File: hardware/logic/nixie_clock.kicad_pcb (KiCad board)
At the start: 2 copper layers, 86 parts, among them J1 Conn_01x06_Pin, J2 Conn_01x04, J3 Conn_02x05_Odd_Even, J4 USB_C_PD, Q1 2N7002NXAKR, Q2 DMP3098LSD-13, SW1 SW_Push, SW2 SW_Push, SW3 SW_Push, SW4 SW_Push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

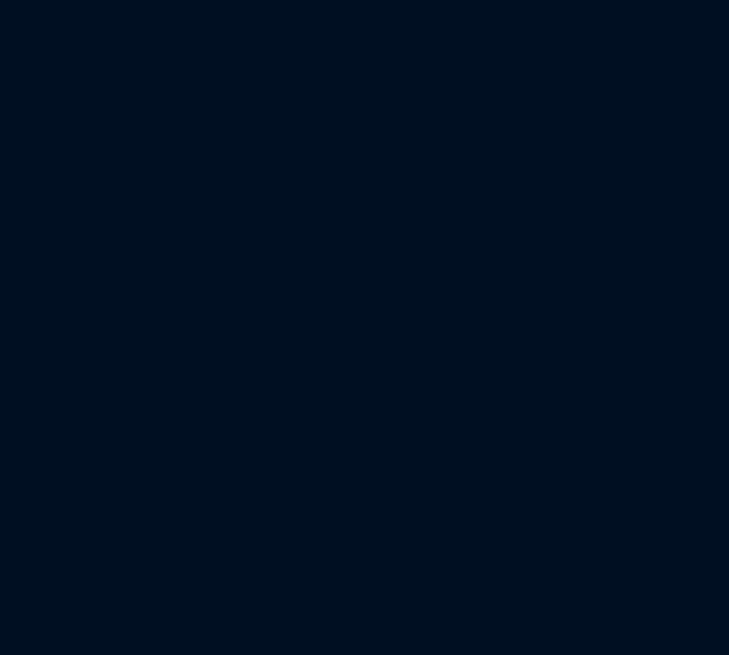
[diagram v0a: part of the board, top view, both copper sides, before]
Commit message: Changed connectors to driver board, fixed oscillator connections
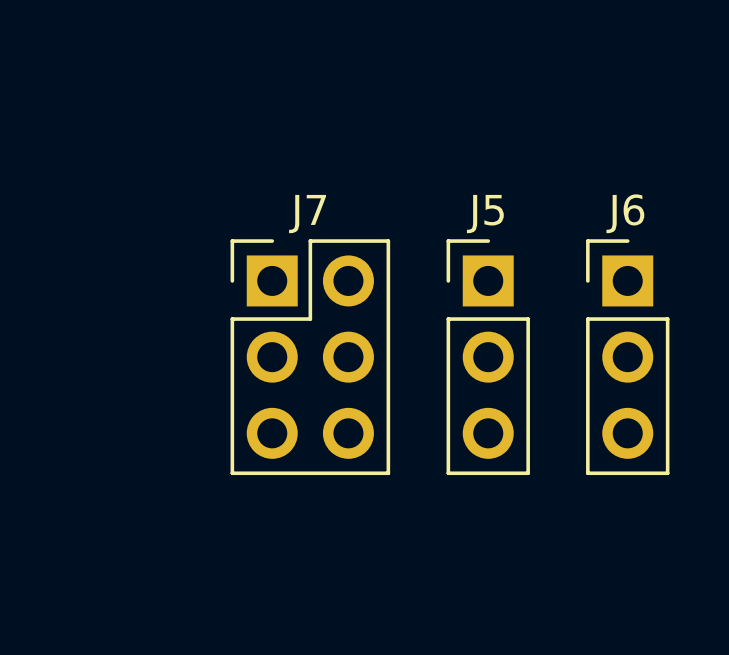
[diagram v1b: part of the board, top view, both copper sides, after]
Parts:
- added J5: Conn_01x03, Connector_PinHeader_2.54mm:PinHeader_1x03_P2.54mm_Vertical, F.Cu at (114.7, 27.9)
- added J6: Conn_01x03, Connector_PinHeader_2.54mm:PinHeader_1x03_P2.54mm_Vertical, F.Cu at (119.4, 27.9)
- added J7: Conn_02x03_Odd_Even, Connector_PinHeader_2.54mm:PinHeader_2x03_P2.54mm_Vertical, F.Cu at (107.5, 27.9)
- R13: value 1k -> 2k2
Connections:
- Y1 pad 2: /nixie_clock-MCU/HSE_IN -> GND
- Y1 pad 3: (no net) -> /nixie_clock-MCU/HSE_IN
- Y1 pad 4: (no net) -> GND

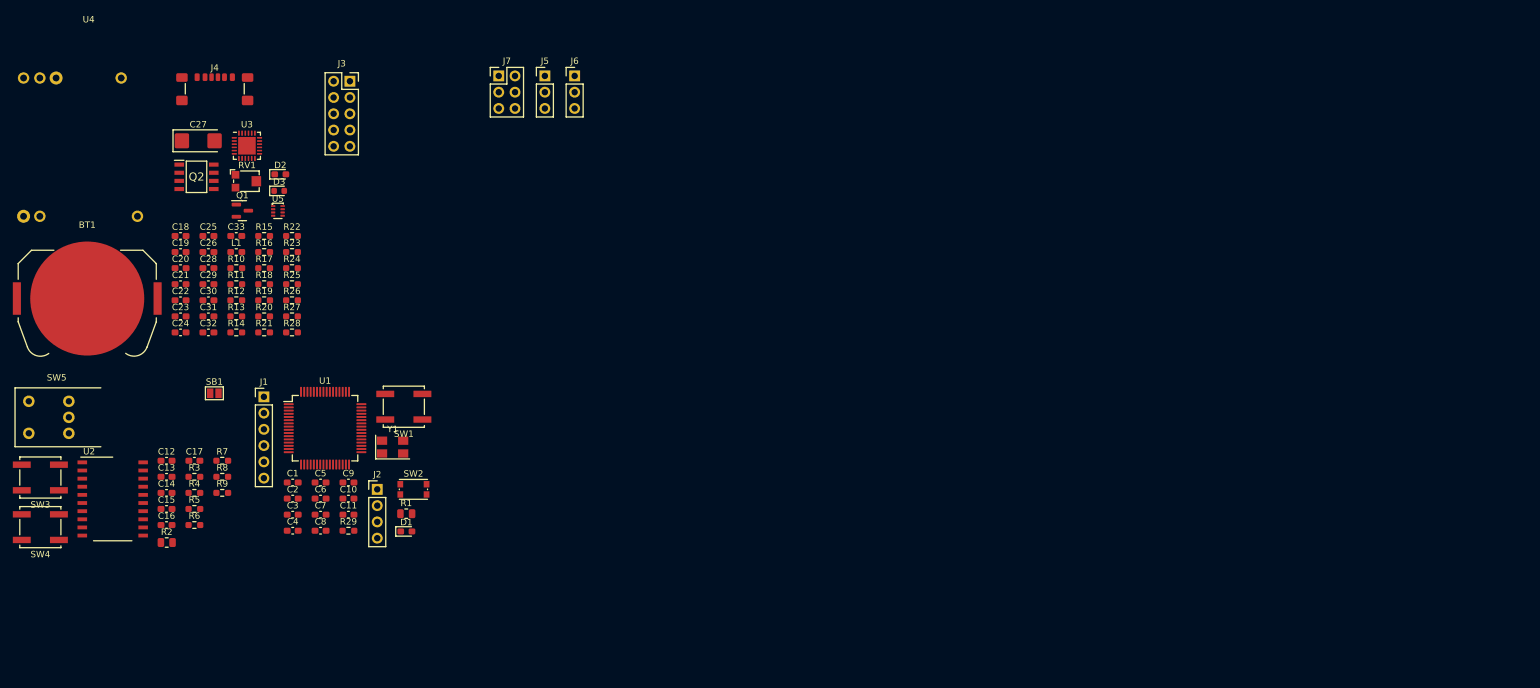
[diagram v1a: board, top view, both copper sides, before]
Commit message: Inital PCB placement
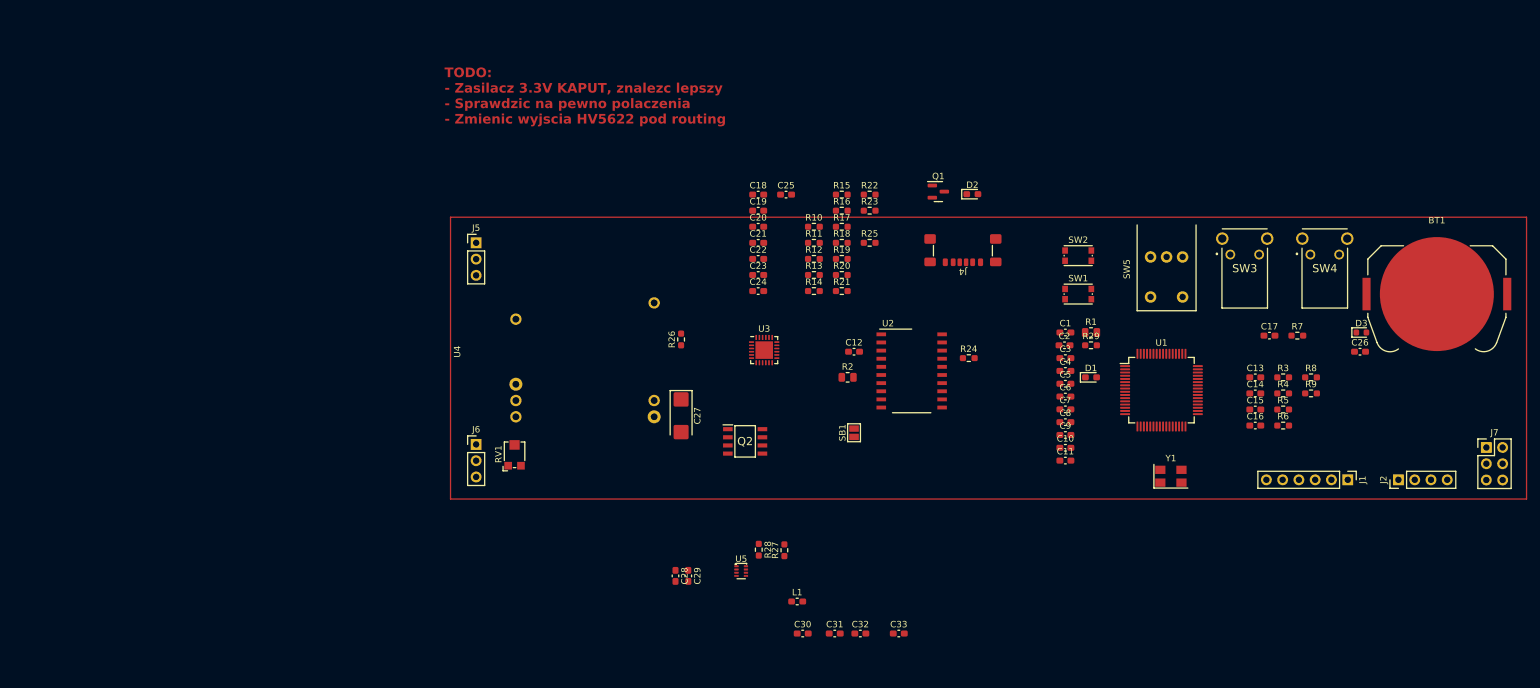
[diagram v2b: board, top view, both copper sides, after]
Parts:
- removed J3: Conn_02x05_Odd_Even, Connector_PinSocket_2.54mm:PinSocket_2x05_P2.54mm_Vertical
- SW1: footprint Button_Switch_SMD:SW_Push_1P1T_NO_CK_KSC6xxJ -> Button_Switch_SMD:SW_Push_1P1T_NO_CK_KMR2
- SW3, SW4: value SW_Push -> FSMRA4JH04; footprint Button_Switch_SMD:SW_Push_1P1T_NO_CK_KSC6xxJ -> FSMRA4JH04:FSMRA4JH04
- moved BT1 210.7 mm to (254.0, 62.0)
- moved SW4 202.8 mm to (234.2, 55.8)
- moved SW3 189.0 mm to (221.8, 55.8)
- moved C26 180.5 mm to (242.0, 71.0)
- moved SW5 176.1 mm to (214.3, 56.2), turned to 90 degrees
- moved C13 170.7 mm to (225.7, 75.0)
- moved C14 170.7 mm to (225.7, 77.5)
- moved C15 170.7 mm to (225.7, 80.0)
- moved C16 170.7 mm to (225.7, 82.5)
- moved R3 170.7 mm to (230.0, 75.0)
- moved R4 170.7 mm to (230.0, 77.5)
- moved R5 170.7 mm to (230.0, 80.0)
- moved R6 170.7 mm to (230.0, 82.5)
- moved R8 170.7 mm to (234.3, 75.0)
- moved R9 170.7 mm to (234.3, 77.5)
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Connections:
- R6 pad 2: Net-(R6-Pad2) -> Net-(R5-Pad2)
- R7 pad 2: Net-(R6-Pad2) -> Net-(R5-Pad2)
- SW5 pad A: Net-(R6-Pad2) -> Net-(R5-Pad2)
- U4 pad 1: VDD -> +HV
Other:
- board text added: "TODO: - Zasilacz 3.3V KAPUT, znalezc lepszy - Sprawdzic na pewno polaczenia - Zmienic wyjscia HV5622 pod routing"

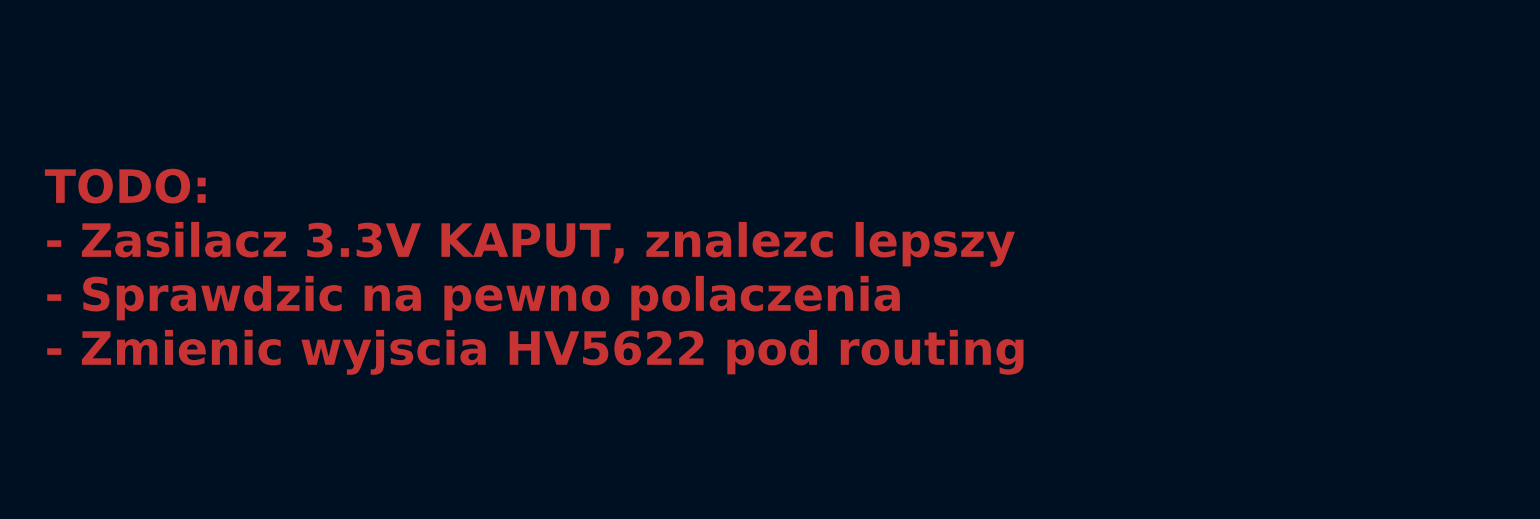
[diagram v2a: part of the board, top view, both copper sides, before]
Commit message: Finish PCB design for nixie_driver
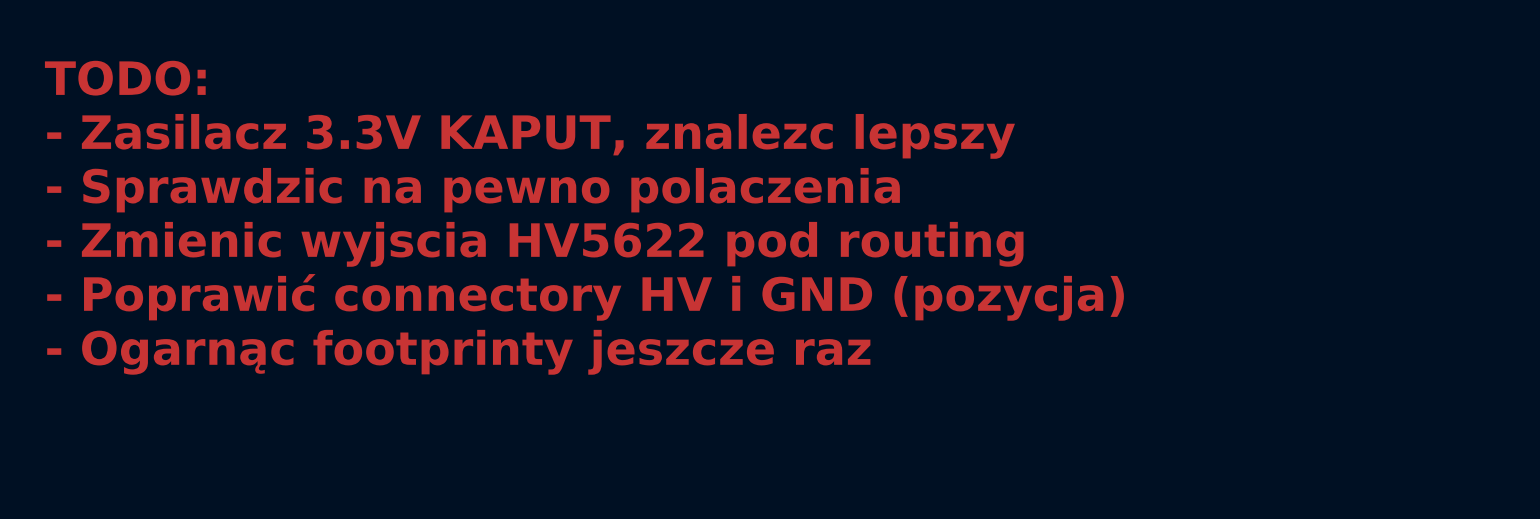
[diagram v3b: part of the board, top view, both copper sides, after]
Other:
- board text added: "TODO: - Zasilacz 3.3V KAPUT, znalezc lepszy - Sprawdzic na pewno polaczenia - Zmienic wyjscia HV5622 pod routing - Poprawić connectory HV i GND (pozycja) - Ogarnąc footprinty jeszcze raz"
- board text removed: "TODO: - Zasilacz 3.3V KAPUT, znalezc lepszy - Sprawdzic na pewno polaczenia - Zmienic wyjscia HV5622 pod routing"
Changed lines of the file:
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@@
   (gr_rect (start 100 50) (end 268 94)
     (stroke (width 0.2) (type default)) (fill none) (layer "F.Cu"))
-  (gr_text "TODO:\n- Zasilacz 3.3V KAPUT, znalezc lepszy\n- Sprawdzic na pewno polaczenia\n- Zmienic wyjscia HV5622 pod routing\n" (at 99.06 35.56) (layer "F.Cu")
+  (gr_text "TODO:\n- Zasilacz 3.3V KAPUT, znalezc lepszy\n- Sprawdzic na pewno polaczenia\n- Zmienic wyjscia HV5622 pod routing\n- Poprawić connectory HV i GND (pozycja)\n- Ogarnąc footprinty jeszcze raz" (at 99.06 35.56) (layer "F.Cu")
     (effects (font (size 1.5 1.5) (thickness 0.3) bold) (justify left bottom))
   )

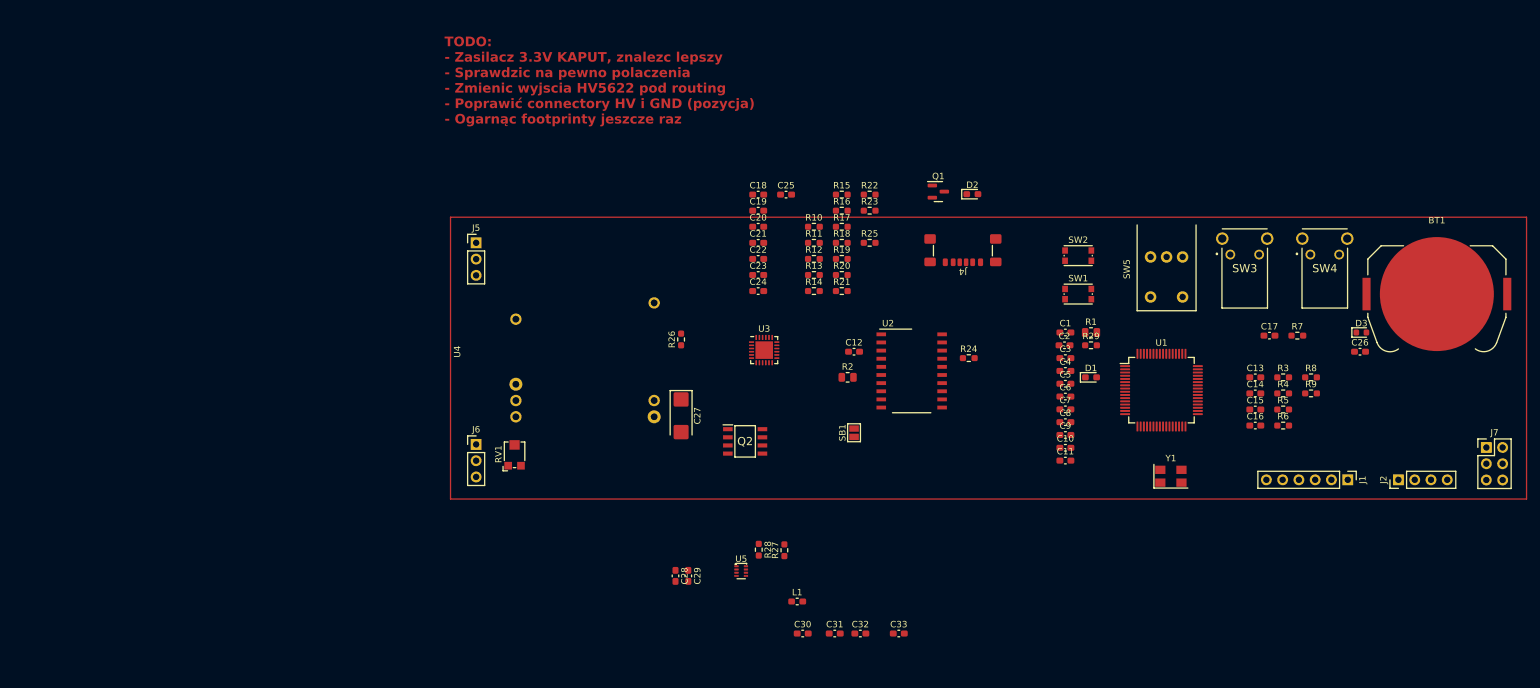
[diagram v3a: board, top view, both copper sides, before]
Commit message: Troubleshooting logic board design, begin component placement, fix positioning of board connectors
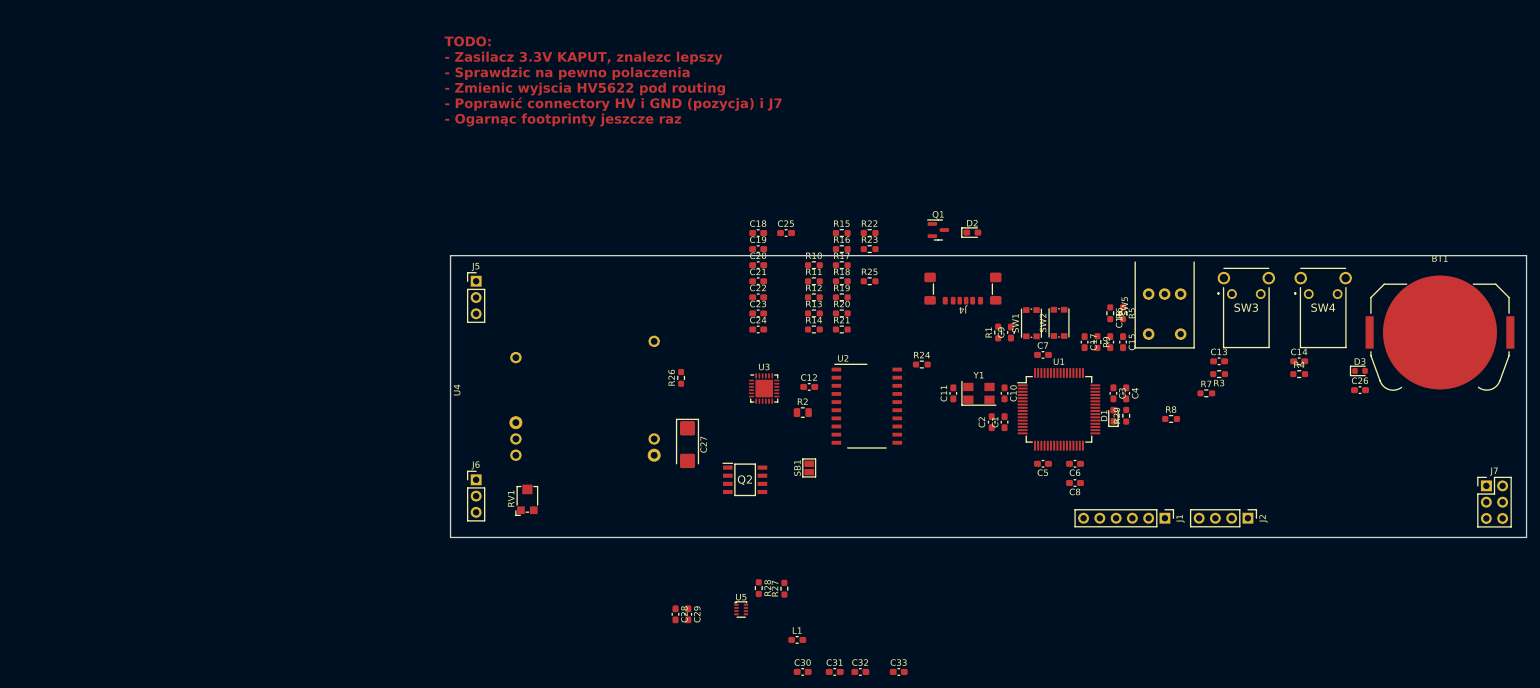
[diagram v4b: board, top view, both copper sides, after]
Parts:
- R1: footprint Resistor_SMD:R_0805_2012Metric -> Resistor_SMD:R_0603_1608Metric_Pad0.98x0.95mm_HandSolder
- SW1: value SW_Push -> SW_RST
- SW2: value SW_Push -> SW_BOOT
- moved R9 34.3 mm to (201.0, 69.5), turned to -90 degrees
- moved Y1 32.6 mm to (182.5, 77.5)
- moved R6 32.2 mm to (203.0, 65.0), turned to -90 degrees
- moved R5 29.2 mm to (205.0, 65.0), turned to -90 degrees
- moved J1 29.2 mm to (211.5, 97.0)
- moved C17 28.9 mm to (199.0, 69.5), turned to -90 degrees
- moved C16 26.1 mm to (203.0, 69.5), turned to -90 degrees
- moved J2 24.3 mm to (224.5, 97.0), turned to -90 degrees
- moved C15 23.2 mm to (205.0, 69.5), turned to -90 degrees
- moved R8 22.8 mm to (212.5, 81.5)
- moved C11 20.4 mm to (178.5, 77.5), turned to 90 degrees
- moved C9 18.1 mm to (187.5, 68.0), turned to -90 degrees
- moved C1 16.9 mm to (186.5, 82.0), turned to 90 degrees
- moved R7 16.8 mm to (218.0, 77.5)
- moved C2 16.5 mm to (184.5, 82.0), turned to 90 degrees
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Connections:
- R6 pad 2: Net-(R5-Pad2) -> Net-(R6-Pad2)
- R7 pad 2: Net-(R5-Pad2) -> Net-(R6-Pad2)
- SW5 pad A: Net-(R5-Pad2) -> Net-(R6-Pad2)
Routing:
- net Net-(BT1-+): track 0.00 -> 0.50 mm
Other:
- board outline added: 168 x 44 mm
- board text added: "TODO: - Zasilacz 3.3V KAPUT, znalezc lepszy - Sprawdzic na pewno polaczenia - Zmienic wyjscia HV5622 pod routing - Poprawić connectory HV i GND (pozycja) i J7 - Ogarnąc footprinty jeszcze raz"
- board text removed: "TODO: - Zasilacz 3.3V KAPUT, znalezc lepszy - Sprawdzic na pewno polaczenia - Zmienic wyjscia HV5622 pod routing - Poprawić connectory HV i GND (pozycja) - Ogarnąc footprinty jeszcze raz"
